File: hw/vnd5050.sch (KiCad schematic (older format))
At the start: 7 parts, among them U401 VND5050AJTR-E

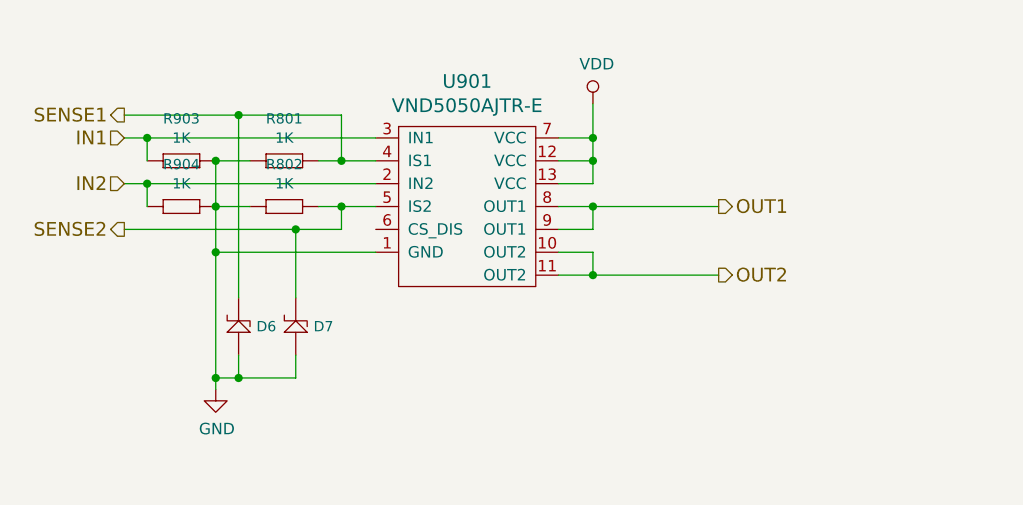
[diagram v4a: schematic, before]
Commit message: pcb 3.5.0 created, added protection diodes for vnd4040 outputs
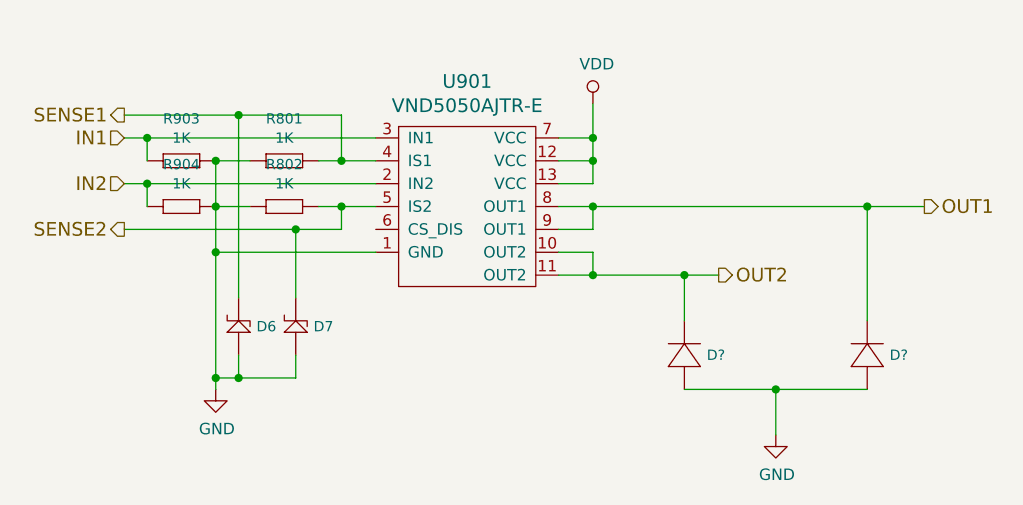
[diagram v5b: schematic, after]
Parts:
- added D? (x2): DIODE_RS07J-GS18, usevolt:DO219AB, symbol usevolt:DIODE_RS07J-GS18
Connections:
- net GND: now also D?.P$1 (P), D?.P$1 (P)
- net OUT1: now also D?.P$2 (N)
- net OUT2: now also D?.P$2 (N)
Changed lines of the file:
@@
 Comment4 ""
 $EndDescr
-Text HLabel 5800 4100 2    60   Output ~ 0
+Text HLabel 6700 4100 2    60   Output ~ 0
 OUT1
 Text HLabel 5800 4400 2    60   Output ~ 0
@@
 	5250 3900 5250 4000
 Wire Wire Line
-	5250 4100 5800 4100
-Wire Wire Line
-	5250 4400 5800 4400
+	5250 4100 6450 4100
+Wire Wire Line
+	5250 4400 5650 4400
 Wire Wire Line
 	3600 4300 3600 4850
@@
 	3600 3900 3750 3900
 Connection ~ 3600 3900
+$Comp
+L usevolt:DIODE_RS07J-GS18 D?
+U 1 1 5C5271C5
+P 5650 4700
+F 0 "D?" V 5600 4602 45  0000 R CNN
+F 1 "DIODE_RS07J-GS18" H 5670 4640 45  0001 L BNN
+F 2 "usevolt:DO219AB" H 5680 4850 20  0001 C CNN
+F 3 "http://www.vishay.com/docs/85742/rs07b.pdf" H 5670 4720 60  0001 C CNN
+F 4 "1864882" H 6270 5320 60  0001 C CNN "2nd Source Part Number"
+F 5 "Digi-Key" H 5970 5020 60  0001 C CNN "1st Source"
+F 6 "Farnell" H 6170 5220 60  0001 C CNN "2nd Source"
+F 7 "RS07J-GS18" H 5870 4920 60  0001 C CNN "Manufacturer Part Number"
+F 8 "RS07J-GS18-ND" H 6070 5120 60  0001 C CNN "1st Source Part Number"
+F 9 "Vishay Semiconductor Diodes Division" H 5770 4820 60  0001 C CNN "Manufacturer"
+	1    5650 4700
+	0    -1   -1   0
+$EndComp
+$Comp
+L usevolt:DIODE_RS07J-GS18 D?
+U 1 1 5C52725E
+P 6450 4700
+F 0 "D?" V 6400 4602 45  0000 R CNN
+F 1 "DIODE_RS07J-GS18" H 6470 4640 45  0001 L BNN
+F 2 "usevolt:DO219AB" H 6480 4850 20  0001 C CNN
+F 3 "http://www.vishay.com/docs/85742/rs07b.pdf" H 6470 4720 60  0001 C CNN
+F 4 "1864882" H 7070 5320 60  0001 C CNN "2nd Source Part Number"
+F 5 "Digi-Key" H 6770 5020 60  0001 C CNN "1st Source"
+F 6 "Farnell" H 6970 5220 60  0001 C CNN "2nd Source"
+F 7 "RS07J-GS18" H 6670 4920 60  0001 C CNN "Manufacturer Part Number"
+F 8 "RS07J-GS18-ND" H 6870 5120 60  0001 C CNN "1st Source Part Number"
+F 9 "Vishay Semiconductor Diodes Division" H 6570 4820 60  0001 C CNN "Manufacturer"
+	1    6450 4700
+	0    -1   -1   0
+$EndComp
+Wire Wire Line
+	6450 4600 6450 4100
+Connection ~ 6450 4100
+Wire Wire Line
+	6450 4100 6700 4100
+Wire Wire Line
+	5650 4600 5650 4400
+Connection ~ 5650 4400
+Wire Wire Line
+	5650 4400 5800 4400
+Wire Wire Line
+	5650 4900 6050 4900
+$Comp
+L power:GND #PWR?
+U 1 1 5C52902F
+P 6050 5100
+F 0 "#PWR?" H 6050 4850 50  0001 C CNN
+F 1 "GND" H 6055 4927 50  0000 C CNN
+F 2 "" H 6050 5100 50  0000 C CNN
+F 3 "" H 6050 5100 50  0000 C CNN
+	1    6050 5100
+	1    0    0    -1
+$EndComp
+Wire Wire Line
+	6050 4900 6050 5100
+Connection ~ 6050 4900
+Wire Wire Line
+	6050 4900 6450 4900
 $EndSCHEMATC

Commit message: silkscreen updated for 3.5.0
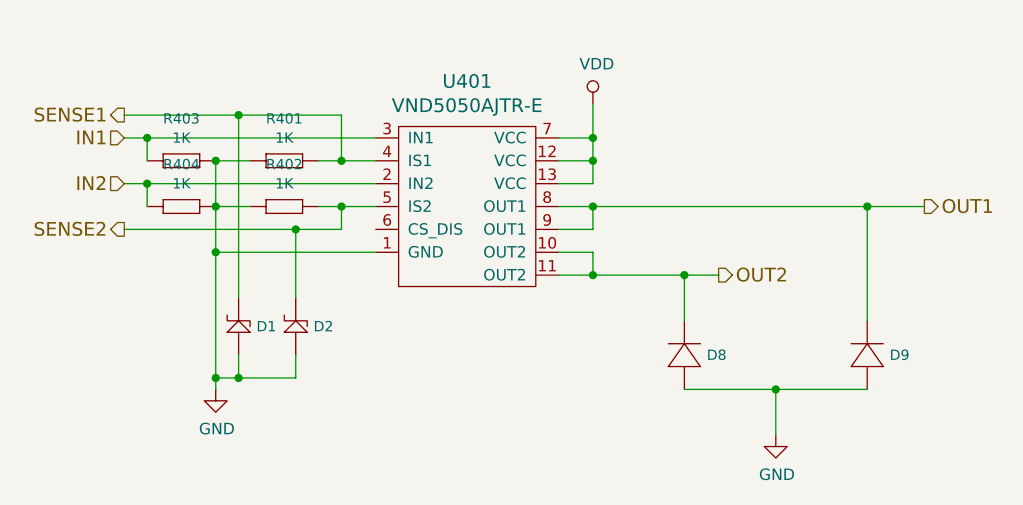
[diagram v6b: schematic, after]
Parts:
- gave numbers to parts that had none: 2
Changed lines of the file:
@@
 AR Path="/5A015FC0/59D8088A" Ref="U401"  Part="1"
 AR Path="/5A02A41F/59D8088A" Ref="U901"  Part="1"
-F 0 "U901" H 4700 4447 60  0000 C CNN
+F 0 "U401" H 4700 4447 60  0000 C CNN
 F 1 "VND5050AJTR-E" H 4700 4341 60  0000 C CNN
 F 2 "usevolt:PowerSSO-12" H 4600 4400 60  0001 C CNN
@@
 AR Path="/5A015FC0/59D808C7" Ref="#PWR0402"  Part="1"
 AR Path="/5A02A41F/59D808C7" Ref="#PWR0802"  Part="1"
-F 0 "#PWR0802" H 5250 3500 50  0001 C CNN
+F 0 "#PWR0402" H 5250 3500 50  0001 C CNN
 F 1 "VDD" H 5267 3823 50  0000 C CNN
 F 2 "" H 5250 3650 50  0000 C CNN
@@
 AR Path="/5A015FC0/59D86DC2" Ref="#PWR0401"  Part="1"
 AR Path="/5A02A41F/59D86DC2" Ref="#PWR0801"  Part="1"
-F 0 "#PWR0801" H 3600 4650 50  0001 C CNN
+F 0 "#PWR0401" H 3600 4650 50  0001 C CNN
 F 1 "GND" H 3605 4727 50  0000 C CNN
 F 2 "" H 3600 4900 50  0000 C CNN
@@
 AR Path="/5A015FC0/5A05950C" Ref="R403"  Part="1"
 AR Path="/5A02A41F/5A05950C" Ref="R903"  Part="1"
-F 0 "R903" H 3450 4084 45  0000 C CNN
+F 0 "R403" H 3450 4084 45  0000 C CNN
 F 1 "1K" H 3450 4000 45  0000 C CNN
 F 2 "yageo:0603" H 3430 4050 20  0001 C CNN
@@
 AR Path="/5A015FC0/5A059568" Ref="R404"  Part="1"
 AR Path="/5A02A41F/5A059568" Ref="R904"  Part="1"
-F 0 "R904" H 3450 4284 45  0000 C CNN
+F 0 "R404" H 3450 4284 45  0000 C CNN
 F 1 "1K" H 3450 4200 45  0000 C CNN
 F 2 "yageo:0603" H 3430 4250 20  0001 C CNN
@@
 AR Path="/5A02A41F/5B1C6487" Ref="R801"  Part="1"
 AR Path="/5A015FC0/5B1C6487" Ref="R401"  Part="1"
-F 0 "R801" H 3900 4084 45  0000 C CNN
+F 0 "R401" H 3900 4084 45  0000 C CNN
 F 1 "1K" H 3900 4000 45  0000 C CNN
 F 2 "yageo:0603" H 3880 4050 20  0001 C CNN
@@
 AR Path="/5A02A41F/5B1C64C1" Ref="R802"  Part="1"
 AR Path="/5A015FC0/5B1C64C1" Ref="R402"  Part="1"
-F 0 "R802" H 3900 4284 45  0000 C CNN
+F 0 "R402" H 3900 4284 45  0000 C CNN
 F 1 "1K" H 3900 4200 45  0000 C CNN
 F 2 "yageo:0603" H 3880 4250 20  0001 C CNN
@@
 AR Path="/5A02A41F/5BAB973C" Ref="D6"  Part="1"
 AR Path="/5A015FC0/5BAB973C" Ref="D1"  Part="1"
-F 0 "D6" V 3625 4472 45  0000 R CNN
+F 0 "D1" V 3625 4472 45  0000 R CNN
 F 1 "ZENER_MM3Z3V6T1G" H 3975 4925 45  0001 L BNN
 F 2 "usevolt:SOD-323" H 3675 4925 20  0001 C CNN
@@
 AR Path="/5A02A41F/5BAB9E63" Ref="D7"  Part="1"
 AR Path="/5A015FC0/5BAB9E63" Ref="D2"  Part="1"
-F 0 "D7" V 3875 4472 45  0000 R CNN
+F 0 "D2" V 3875 4472 45  0000 R CNN
 F 1 "ZENER_MM3Z3V6T1G" H 4225 4925 45  0001 L BNN
 F 2 "usevolt:SOD-323" H 3925 4925 20  0001 C CNN
@@
 Connection ~ 3600 3900
 $Comp
-L usevolt:DIODE_RS07J-GS18 D?
+L usevolt:DIODE_RS07J-GS18 D10
 U 1 1 5C5271C5
 P 5650 4700
-F 0 "D?" V 5600 4602 45  0000 R CNN
+AR Path="/5A02A41F/5C5271C5" Ref="D10"  Part="1"
+AR Path="/5A015FC0/5C5271C5" Ref="D8"  Part="1"
+F 0 "D8" V 5600 4602 45  0000 R CNN
 F 1 "DIODE_RS07J-GS18" H 5670 4640 45  0001 L BNN
 F 2 "usevolt:DO219AB" H 5680 4850 20  0001 C CNN
@@
 $EndComp
 $Comp
-L usevolt:DIODE_RS07J-GS18 D?
+L usevolt:DIODE_RS07J-GS18 D11
 U 1 1 5C52725E
 P 6450 4700
-F 0 "D?" V 6400 4602 45  0000 R CNN
+AR Path="/5A02A41F/5C52725E" Ref="D11"  Part="1"
+AR Path="/5A015FC0/5C52725E" Ref="D9"  Part="1"
+F 0 "D9" V 6400 4602 45  0000 R CNN
 F 1 "DIODE_RS07J-GS18" H 6470 4640 45  0001 L BNN
 F 2 "usevolt:DO219AB" H 6480 4850 20  0001 C CNN
@@
 	5650 4900 6050 4900
 $Comp
-L power:GND #PWR?
+L power:GND #PWR0111
 U 1 1 5C52902F
 P 6050 5100
-F 0 "#PWR?" H 6050 4850 50  0001 C CNN
+AR Path="/5A02A41F/5C52902F" Ref="#PWR0111"  Part="1"
+AR Path="/5A015FC0/5C52902F" Ref="#PWR0110"  Part="1"
+F 0 "#PWR0110" H 6050 4850 50  0001 C CNN
 F 1 "GND" H 6055 4927 50  0000 C CNN
 F 2 "" H 6050 5100 50  0000 C CNN

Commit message: pcb 3.6.0 created, with double fets in work & drive lights
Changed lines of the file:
@@
 AR Path="/5A015FC0/59D8088A" Ref="U401"  Part="1"
 AR Path="/5A02A41F/59D8088A" Ref="U901"  Part="1"
-F 0 "U401" H 4700 4447 60  0000 C CNN
+F 0 "U901" H 4700 4447 60  0000 C CNN
 F 1 "VND5050AJTR-E" H 4700 4341 60  0000 C CNN
 F 2 "usevolt:PowerSSO-12" H 4600 4400 60  0001 C CNN
@@
 AR Path="/5A015FC0/59D808C7" Ref="#PWR0402"  Part="1"
 AR Path="/5A02A41F/59D808C7" Ref="#PWR0802"  Part="1"
-F 0 "#PWR0402" H 5250 3500 50  0001 C CNN
+F 0 "#PWR0802" H 5250 3500 50  0001 C CNN
 F 1 "VDD" H 5267 3823 50  0000 C CNN
 F 2 "" H 5250 3650 50  0000 C CNN
@@
 AR Path="/5A015FC0/59D86DC2" Ref="#PWR0401"  Part="1"
 AR Path="/5A02A41F/59D86DC2" Ref="#PWR0801"  Part="1"
-F 0 "#PWR0401" H 3600 4650 50  0001 C CNN
+F 0 "#PWR0801" H 3600 4650 50  0001 C CNN
 F 1 "GND" H 3605 4727 50  0000 C CNN
 F 2 "" H 3600 4900 50  0000 C CNN
@@
 AR Path="/5A015FC0/5A05950C" Ref="R403"  Part="1"
 AR Path="/5A02A41F/5A05950C" Ref="R903"  Part="1"
-F 0 "R403" H 3450 4084 45  0000 C CNN
+F 0 "R903" H 3450 4084 45  0000 C CNN
 F 1 "1K" H 3450 4000 45  0000 C CNN
 F 2 "yageo:0603" H 3430 4050 20  0001 C CNN
@@
 AR Path="/5A015FC0/5A059568" Ref="R404"  Part="1"
 AR Path="/5A02A41F/5A059568" Ref="R904"  Part="1"
-F 0 "R404" H 3450 4284 45  0000 C CNN
+F 0 "R904" H 3450 4284 45  0000 C CNN
 F 1 "1K" H 3450 4200 45  0000 C CNN
 F 2 "yageo:0603" H 3430 4250 20  0001 C CNN
@@
 AR Path="/5A02A41F/5B1C6487" Ref="R801"  Part="1"
 AR Path="/5A015FC0/5B1C6487" Ref="R401"  Part="1"
-F 0 "R401" H 3900 4084 45  0000 C CNN
+F 0 "R801" H 3900 4084 45  0000 C CNN
 F 1 "1K" H 3900 4000 45  0000 C CNN
 F 2 "yageo:0603" H 3880 4050 20  0001 C CNN
@@
 AR Path="/5A02A41F/5B1C64C1" Ref="R802"  Part="1"
 AR Path="/5A015FC0/5B1C64C1" Ref="R402"  Part="1"
-F 0 "R402" H 3900 4284 45  0000 C CNN
+F 0 "R802" H 3900 4284 45  0000 C CNN
 F 1 "1K" H 3900 4200 45  0000 C CNN
 F 2 "yageo:0603" H 3880 4250 20  0001 C CNN
@@
 AR Path="/5A02A41F/5BAB973C" Ref="D6"  Part="1"
 AR Path="/5A015FC0/5BAB973C" Ref="D1"  Part="1"
-F 0 "D1" V 3625 4472 45  0000 R CNN
+F 0 "D6" V 3625 4472 45  0000 R CNN
 F 1 "ZENER_MM3Z3V6T1G" H 3975 4925 45  0001 L BNN
 F 2 "usevolt:SOD-323" H 3675 4925 20  0001 C CNN
@@
 AR Path="/5A02A41F/5BAB9E63" Ref="D7"  Part="1"
 AR Path="/5A015FC0/5BAB9E63" Ref="D2"  Part="1"
-F 0 "D2" V 3875 4472 45  0000 R CNN
+F 0 "D7" V 3875 4472 45  0000 R CNN
 F 1 "ZENER_MM3Z3V6T1G" H 4225 4925 45  0001 L BNN
 F 2 "usevolt:SOD-323" H 3925 4925 20  0001 C CNN
@@
 AR Path="/5A02A41F/5C5271C5" Ref="D10"  Part="1"
 AR Path="/5A015FC0/5C5271C5" Ref="D8"  Part="1"
-F 0 "D8" V 5600 4602 45  0000 R CNN
+F 0 "D10" V 5600 4602 45  0000 R CNN
 F 1 "DIODE_RS07J-GS18" H 5670 4640 45  0001 L BNN
 F 2 "usevolt:DO219AB" H 5680 4850 20  0001 C CNN
@@
 AR Path="/5A02A41F/5C52725E" Ref="D11"  Part="1"
 AR Path="/5A015FC0/5C52725E" Ref="D9"  Part="1"
-F 0 "D9" V 6400 4602 45  0000 R CNN
+F 0 "D11" V 6400 4602 45  0000 R CNN
 F 1 "DIODE_RS07J-GS18" H 6470 4640 45  0001 L BNN
 F 2 "usevolt:DO219AB" H 6480 4850 20  0001 C CNN
@@
 AR Path="/5A02A41F/5C52902F" Ref="#PWR0111"  Part="1"
 AR Path="/5A015FC0/5C52902F" Ref="#PWR0110"  Part="1"
-F 0 "#PWR0110" H 6050 4850 50  0001 C CNN
+F 0 "#PWR0111" H 6050 4850 50  0001 C CNN
 F 1 "GND" H 6055 4927 50  0000 C CNN
 F 2 "" H 6050 5100 50  0000 C CNN
